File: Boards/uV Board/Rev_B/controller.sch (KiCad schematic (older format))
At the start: 3 parts

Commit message: Created analog in sheets on ADC board, populated them, and connected them to controller.  Defined Interconnect pins. Placed mounting holes.
Converted some strain gauge connections to nets.
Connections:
- net Analog1 is gone; now on net A7: J?.2 (Pin_2)
- net Analog2 is gone; now on net A6: J?.3 (Pin_3)
- net DIO1 is gone; now on net D12: J?.5 (Pin_5)
- net DIO2 is gone; now on net D11: J?.4 (Pin_4)
- net D11: now reaches J?.14 (Pin_14)
- net D12: now reaches J?.15 (Pin_15)
- net A7: now reaches J?.5 (Pin_5)
- net A6: now reaches J?.6 (Pin_6)
- no-connect marks 20 -> 16
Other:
- note added: "D11\n"
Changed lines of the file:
@@
 NoConn ~ 2600 2150
 NoConn ~ 2600 2050
-NoConn ~ 2600 1350
-NoConn ~ 2600 1250
 NoConn ~ 2600 1150
 NoConn ~ 2600 1050
@@
 Text HLabel 4000 950  0    50   Input ~ 0
 5V
+Text Label 4500 1150 0    50   ~ 0
+D11
 Text Label 4500 1050 0    50   ~ 0
-DIO1
-Text Label 4500 1150 0    50   ~ 0
-DIO2
+D12
 Text Label 4000 1050 2    50   ~ 0
-Analog1
+A7
 Text Label 4000 1150 2    50   ~ 0
-Analog2
+A6
 Text HLabel 4500 950  2    50   Input ~ 0
 GND
@@
 NoConn ~ 2600 2250
 NoConn ~ 1400 2050
-NoConn ~ 1400 2150
-NoConn ~ 1400 2250
 Text Notes 2350 1050 0    50   ~ 0
 Reset\n
@@
 Wire Notes Line
 	1100 700  3500 700
+Text Label 2600 1250 2    50   ~ 0
+A7
+Text Label 2600 1350 2    50   ~ 0
+A6
+Text Label 1400 2150 2    50   ~ 0
+D11
+Text Label 1400 2250 2    50   ~ 0
+D12
+Text Notes 1650 2200 0    50   ~ 0
+D11\n
 $EndSCHEMATC

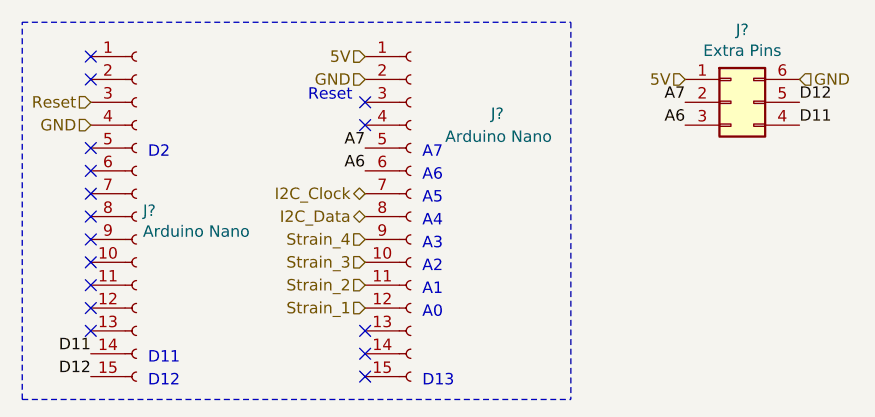
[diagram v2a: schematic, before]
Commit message: Fixed regulator nonsense on ADC board. Rules checked both ADC and micro boards. Fixed interconnect on ADC board.
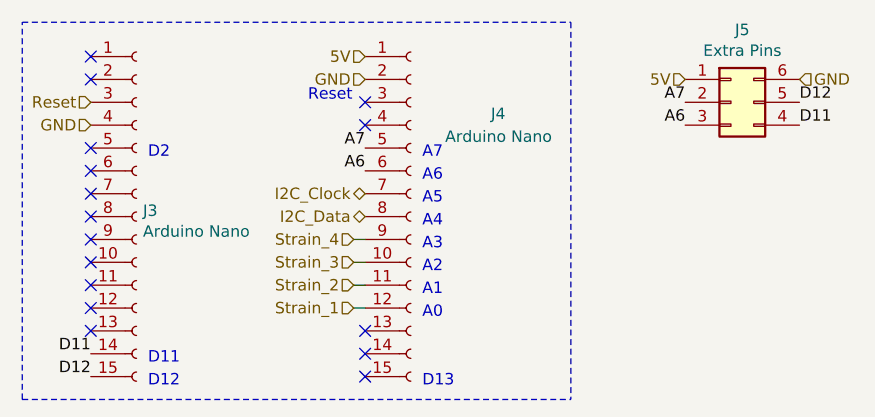
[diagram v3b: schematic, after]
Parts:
- gave numbers to parts that had none: 3
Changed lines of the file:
@@
 $EndDescr
 $Comp
-L Connector:Conn_01x15_Female J?
+L Connector:Conn_01x15_Female J3
 U 1 1 614FE43E
 P 1600 1550
-F 0 "J?" H 1628 1576 50  0000 L CNN
+F 0 "J3" H 1628 1576 50  0000 L CNN
 F 1 "Arduino Nano" H 1628 1485 50  0000 L CNN
 F 2 "" H 1600 1550 50  0001 C CNN
@@
 NoConn ~ 2600 1050
 $Comp
-L Connector:Conn_01x15_Female J?
+L Connector:Conn_01x15_Female J4
 U 1 1 61504D87
 P 2800 1550
-F 0 "J?" H 3150 2000 50  0000 L CNN
+F 0 "J4" H 3150 2000 50  0000 L CNN
 F 1 "Arduino Nano" H 2950 1900 50  0000 L CNN
 F 2 "" H 2800 1550 50  0001 C CNN
@@
 $EndComp
 $Comp
-L Connector_Generic:Conn_02x03_Counter_Clockwise J?
+L Connector_Generic:Conn_02x03_Counter_Clockwise J5
 U 1 1 61567E78
 P 4200 1050
-F 0 "J?" H 4250 1367 50  0000 C CNN
+F 0 "J5" H 4250 1367 50  0000 C CNN
 F 1 "Extra Pins" H 4250 1276 50  0000 C CNN
 F 2 "" H 4200 1050 50  0001 C CNN
@@
 Text HLabel 4500 950  2    50   Input ~ 0
 GND
-Text HLabel 2600 1650 0    50   Input ~ 0
+Text HLabel 2550 1650 0    50   Input ~ 0
 Strain_4
-Text HLabel 2600 1750 0    50   Input ~ 0
+Text HLabel 2550 1750 0    50   Input ~ 0
 Strain_3
-Text HLabel 2600 1850 0    50   Input ~ 0
+Text HLabel 2550 1850 0    50   Input ~ 0
 Strain_2
-Text HLabel 2600 1950 0    50   Input ~ 0
+Text HLabel 2550 1950 0    50   Input ~ 0
 Strain_1
 NoConn ~ 2600 2250
@@
 Text Notes 1650 2200 0    50   ~ 0
 D11\n
+Wire Wire Line
+	2550 1650 2600 1650
+Wire Wire Line
+	2600 1750 2550 1750
+Wire Wire Line
+	2600 1850 2550 1850
+Wire Wire Line
+	2600 1950 2550 1950
 $EndSCHEMATC

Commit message: Moved around components on the ADC board PCB. Assigned footprints to microVolt board components.
Tried to add 6-pin spring connector to custom schematics list.
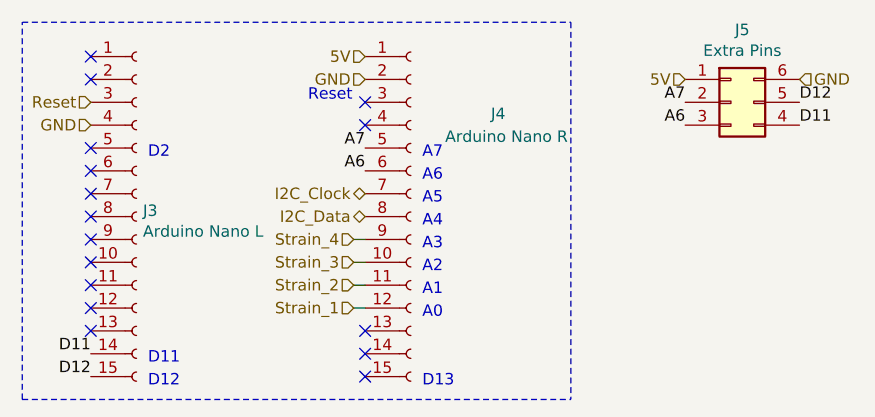
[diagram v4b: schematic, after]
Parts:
- J3: value Arduino Nano -> Arduino Nano L; footprint (none) -> Connector_PinHeader_2.54mm:PinHeader_1x15_P2.54mm_Vertical
- J4: value Arduino Nano -> Arduino Nano R; footprint (none) -> Connector_PinHeader_2.54mm:PinHeader_1x15_P2.54mm_Vertical
- J5: footprint (none) -> Connector_PinHeader_2.54mm:PinHeader_2x03_P2.54mm_Vertical
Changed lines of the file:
@@
 P 1600 1550
 F 0 "J3" H 1628 1576 50  0000 L CNN
-F 1 "Arduino Nano" H 1628 1485 50  0000 L CNN
-F 2 "" H 1600 1550 50  0001 C CNN
+F 1 "Arduino Nano L" H 1628 1485 50  0000 L CNN
+F 2 "Connector_PinHeader_2.54mm:PinHeader_1x15_P2.54mm_Vertical" H 1600 1550 50  0001 C CNN
 F 3 "~" H 1600 1550 50  0001 C CNN
 	1    1600 1550
@@
 P 2800 1550
 F 0 "J4" H 3150 2000 50  0000 L CNN
-F 1 "Arduino Nano" H 2950 1900 50  0000 L CNN
-F 2 "" H 2800 1550 50  0001 C CNN
+F 1 "Arduino Nano R" H 2950 1900 50  0000 L CNN
+F 2 "Connector_PinHeader_2.54mm:PinHeader_1x15_P2.54mm_Vertical" H 2800 1550 50  0001 C CNN
 F 3 "~" H 2800 1550 50  0001 C CNN
 	1    2800 1550
@@
 F 0 "J5" H 4250 1367 50  0000 C CNN
 F 1 "Extra Pins" H 4250 1276 50  0000 C CNN
-F 2 "" H 4200 1050 50  0001 C CNN
+F 2 "Connector_PinHeader_2.54mm:PinHeader_2x03_P2.54mm_Vertical" H 4200 1050 50  0001 C CNN
 F 3 "~" H 4200 1050 50  0001 C CNN
 	1    4200 1050

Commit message: Created and layed out most of PCB for microvolt board. Removed one strain module, and added multiple mounting holes for the boards to be placed on.
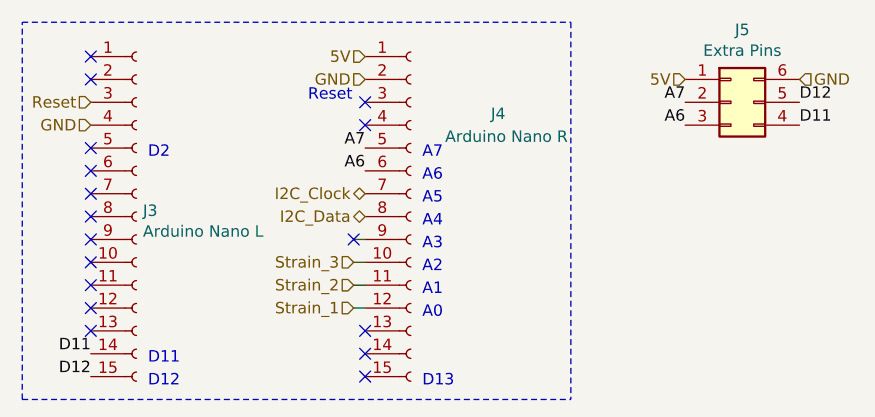
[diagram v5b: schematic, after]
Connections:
- net Strain_4: no longer names the net of J4.9 (Pin_9)
- no-connect marks 16 -> 17
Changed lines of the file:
@@
 Text HLabel 4500 950  2    50   Input ~ 0
 GND
-Text HLabel 2550 1650 0    50   Input ~ 0
-Strain_4
 Text HLabel 2550 1750 0    50   Input ~ 0
 Strain_3
@@
 Wire Wire Line
 	2600 1950 2550 1950
+NoConn ~ 2550 1650
 $EndSCHEMATC
